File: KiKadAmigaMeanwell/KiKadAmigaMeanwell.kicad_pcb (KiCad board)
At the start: 2 copper layers, 99 x 148.5 mm, 11 parts

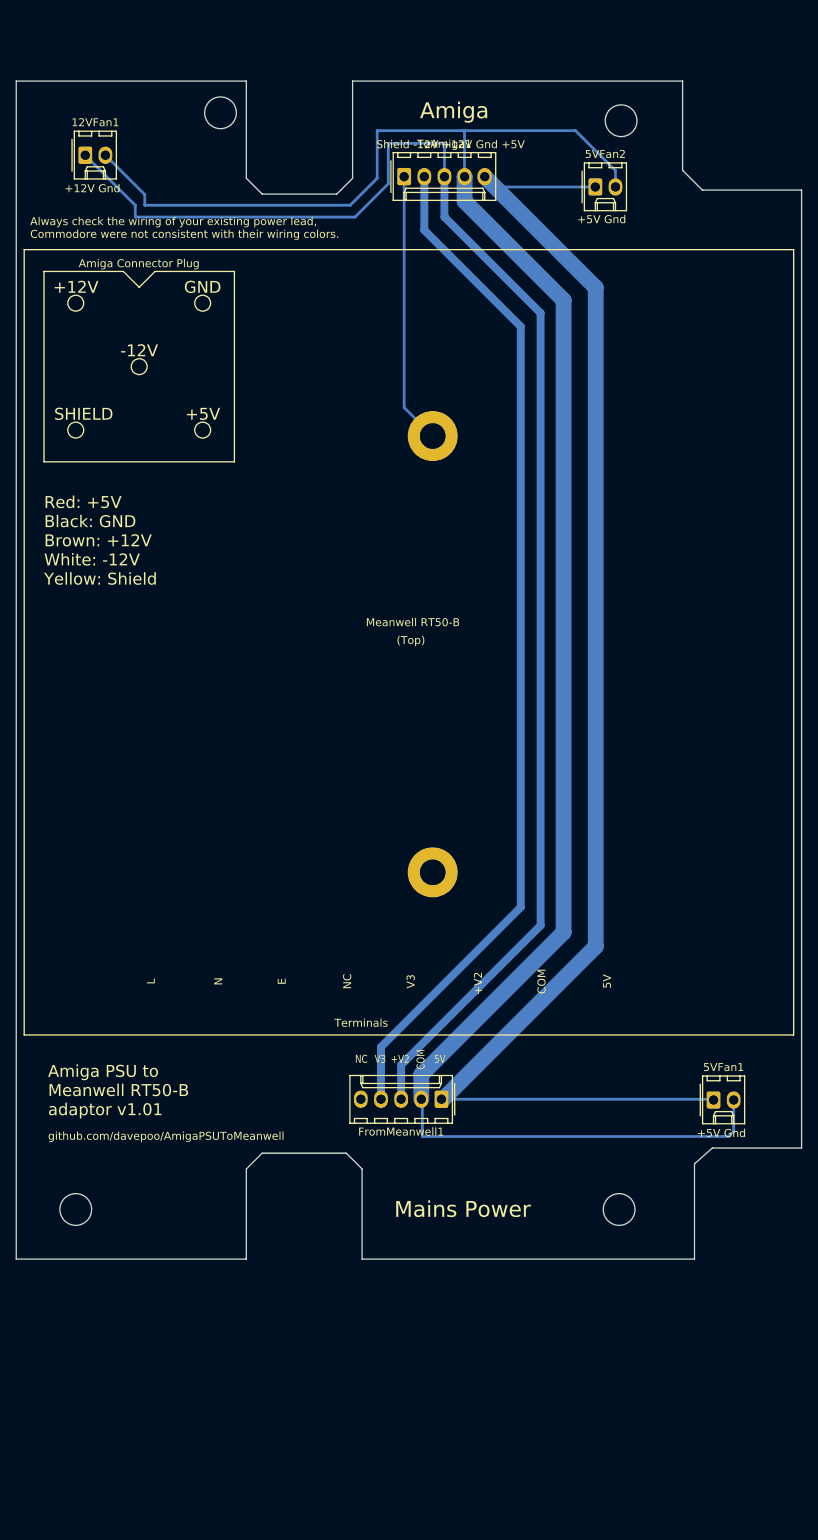
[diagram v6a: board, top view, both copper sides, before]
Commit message: - taking 0.2mm off the left hand edge cut & correcting silkscreen errors
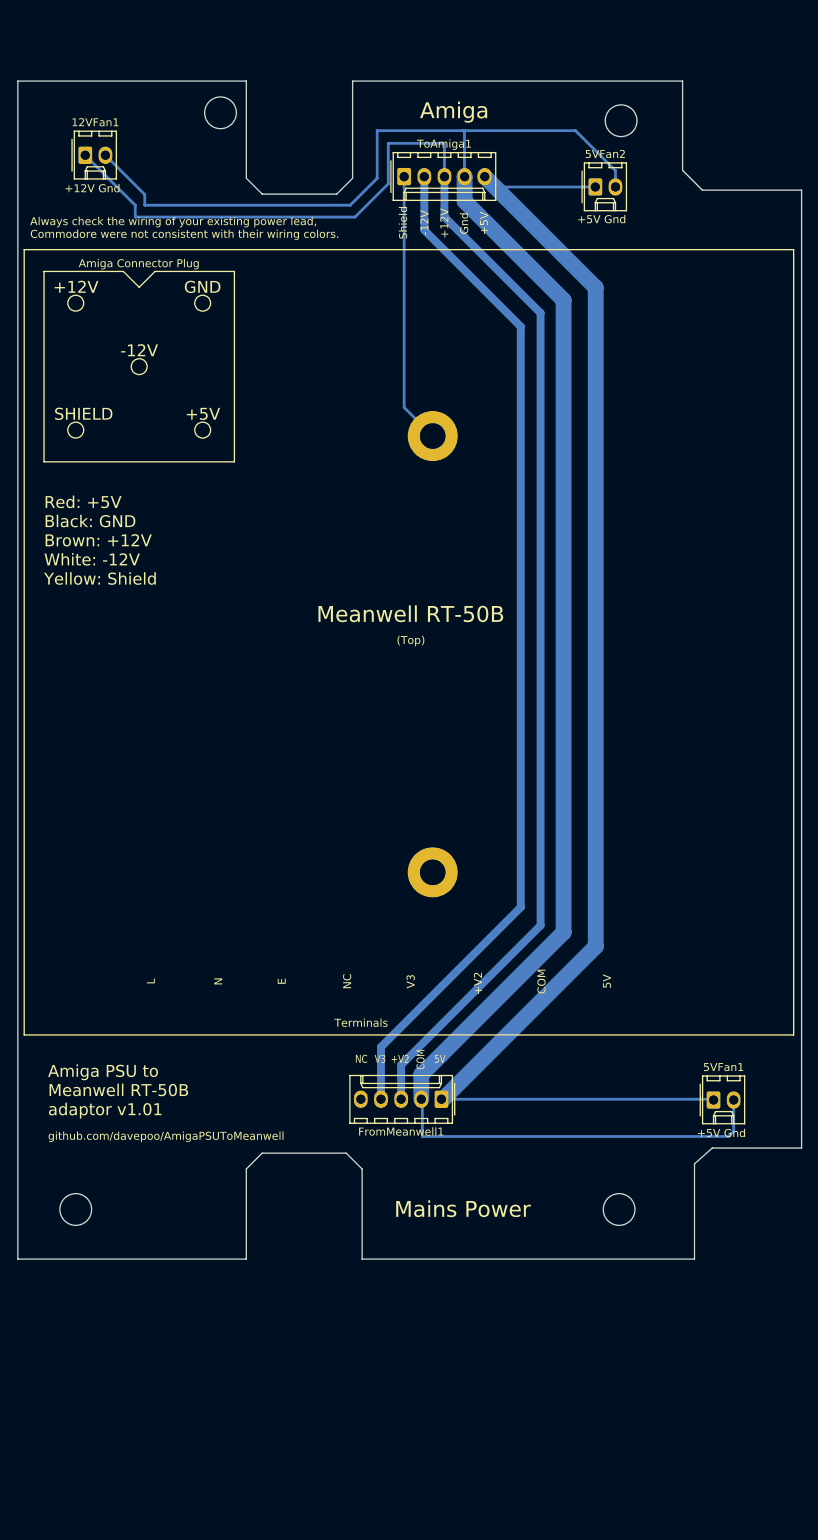
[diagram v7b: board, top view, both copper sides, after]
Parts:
- Meanwell RT-50B: renamed from Meanwell RT50-B
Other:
- board size 99 x 148.5 mm -> 98.8 x 148.5 mm
- board text added: "+12V"
- board text added: "+5V"
- board text added: "-12V"
- board text added: "Amiga PSU to Meanwell RT-50B adaptor v1.01"
- board text added: "Gnd"
- board text added: "Shield"
- board text removed: "Amiga PSU to Meanwell RT50-B adaptor v1.01"
- board text removed: "Shield -12V +12V Gnd +5V"
